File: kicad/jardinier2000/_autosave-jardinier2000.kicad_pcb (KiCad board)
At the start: 2 copper layers, 53 parts, among them J1 5V, J10 I2C, J11 I2C, J2 VIN Reg, J3 5V, J4 5V, J5 5V, J6 5_30V, J7 I2C, J8 5V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

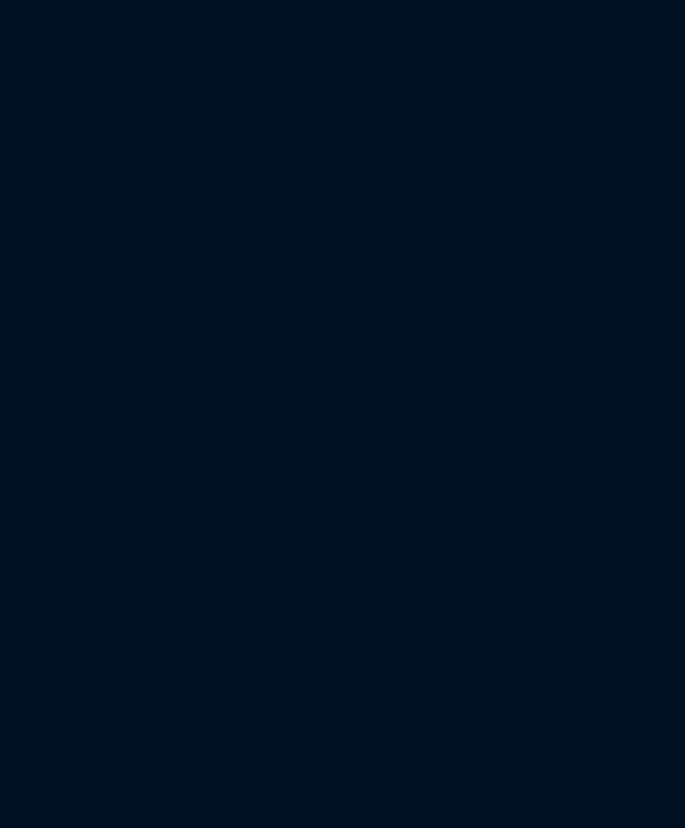
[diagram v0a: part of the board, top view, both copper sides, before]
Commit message: Update bazel version
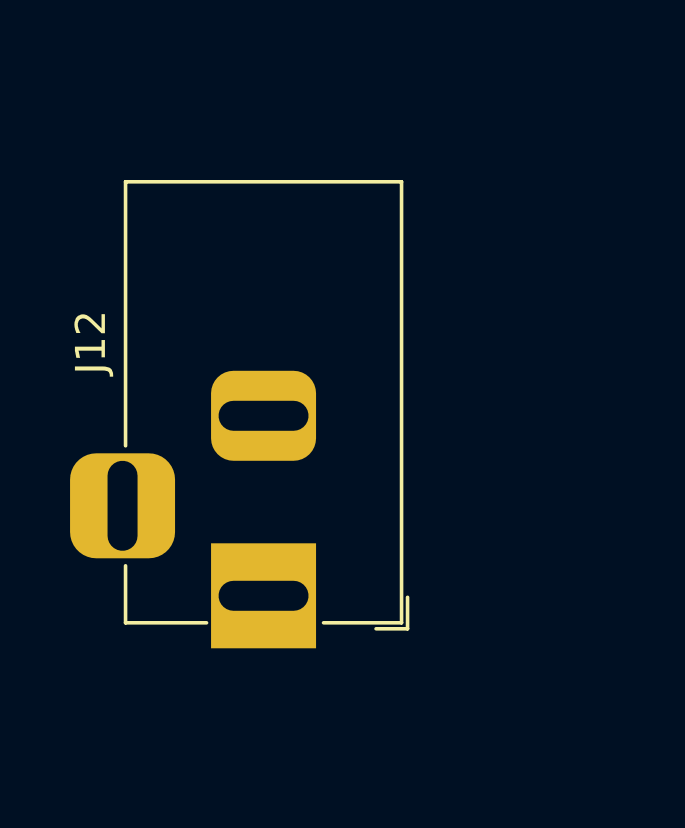
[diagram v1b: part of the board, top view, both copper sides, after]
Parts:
- added J12: Barrel_Jack_Switch, Connector_BarrelJack:BarrelJack_Horizontal, F.Cu at (97.0, 121.0)
